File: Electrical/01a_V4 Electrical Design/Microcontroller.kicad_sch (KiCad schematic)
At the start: 25 parts, among them J2 M20-7920242R, Q1 XP231P0201TR-G, U1 STM32F446RETx, Y1 16Mhz, 3.2 x 2.5

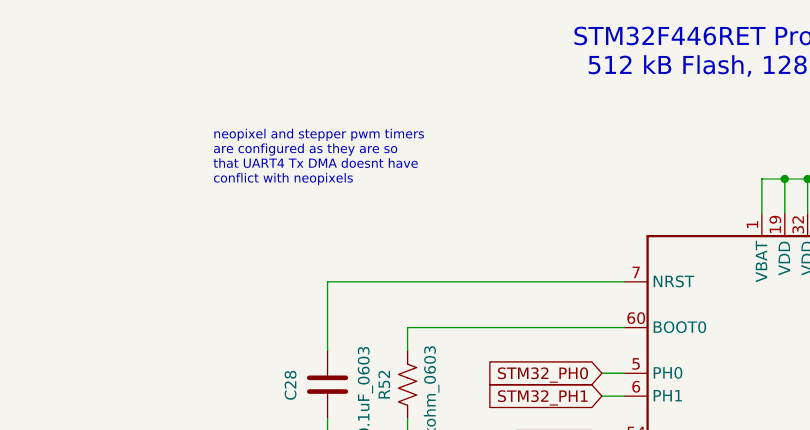
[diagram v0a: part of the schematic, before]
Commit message: main schematic tweaks. Started the 'Saber' PCB which is the new end effector for the strobe light. Schematic nearly finished. Need to create footprint for LEDs and layout the board to be CNC milled.
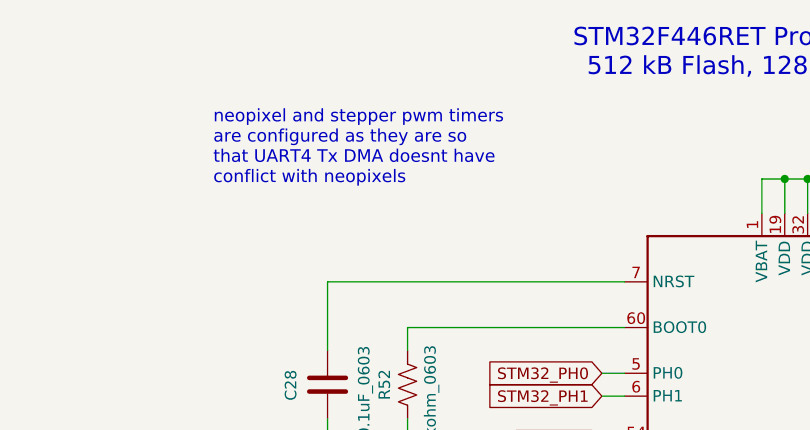
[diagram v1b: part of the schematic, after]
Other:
- company: (none) -> Kadin Whiting
- title: (none) -> STM32 Microcontroller
